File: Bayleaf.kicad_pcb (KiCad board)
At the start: 2 copper layers, 297 x 94.2 mm, 142 parts

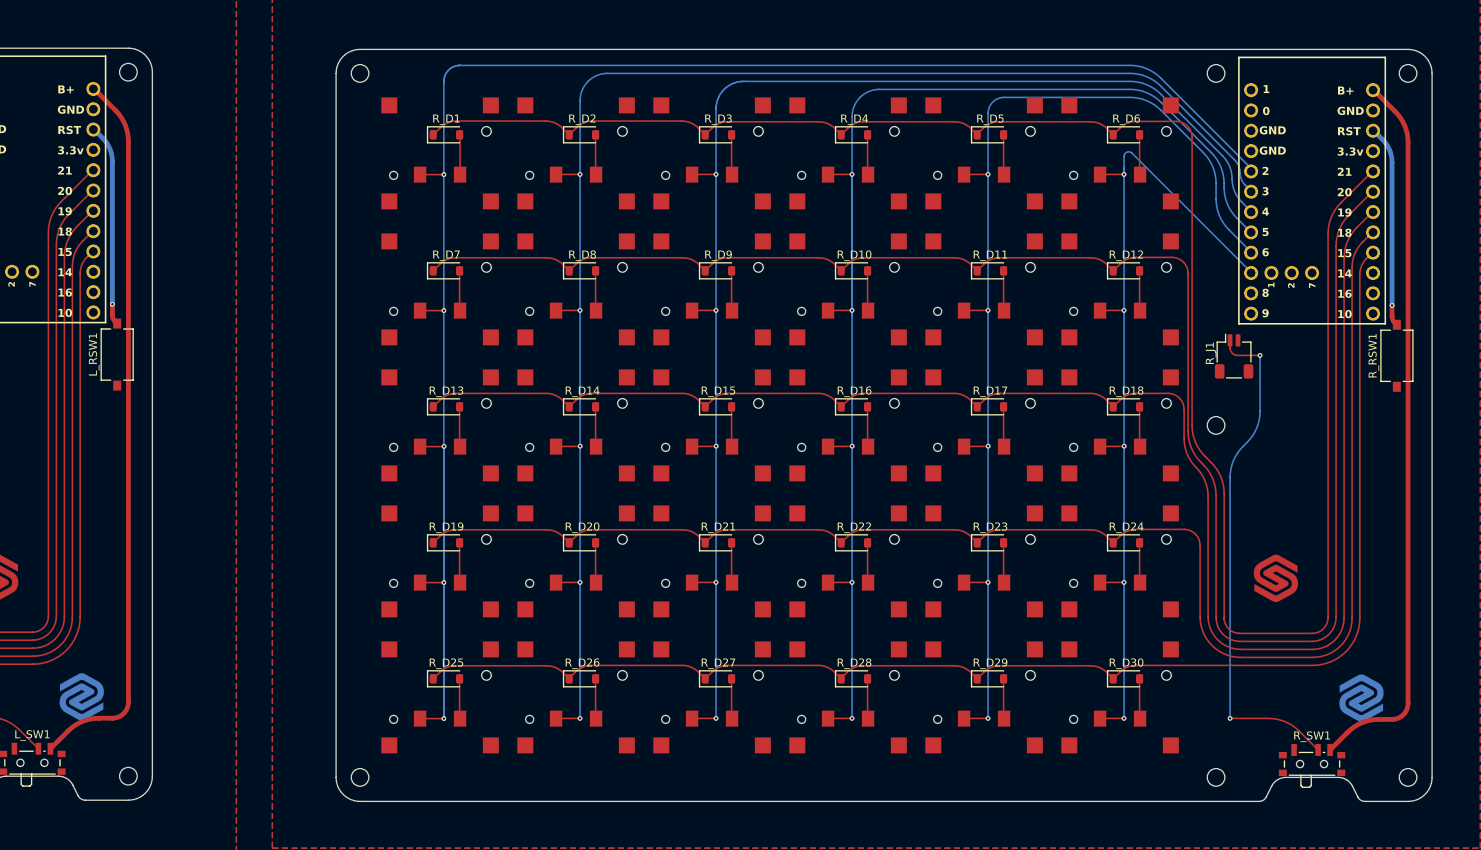
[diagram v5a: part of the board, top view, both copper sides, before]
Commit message: Connect traces on right
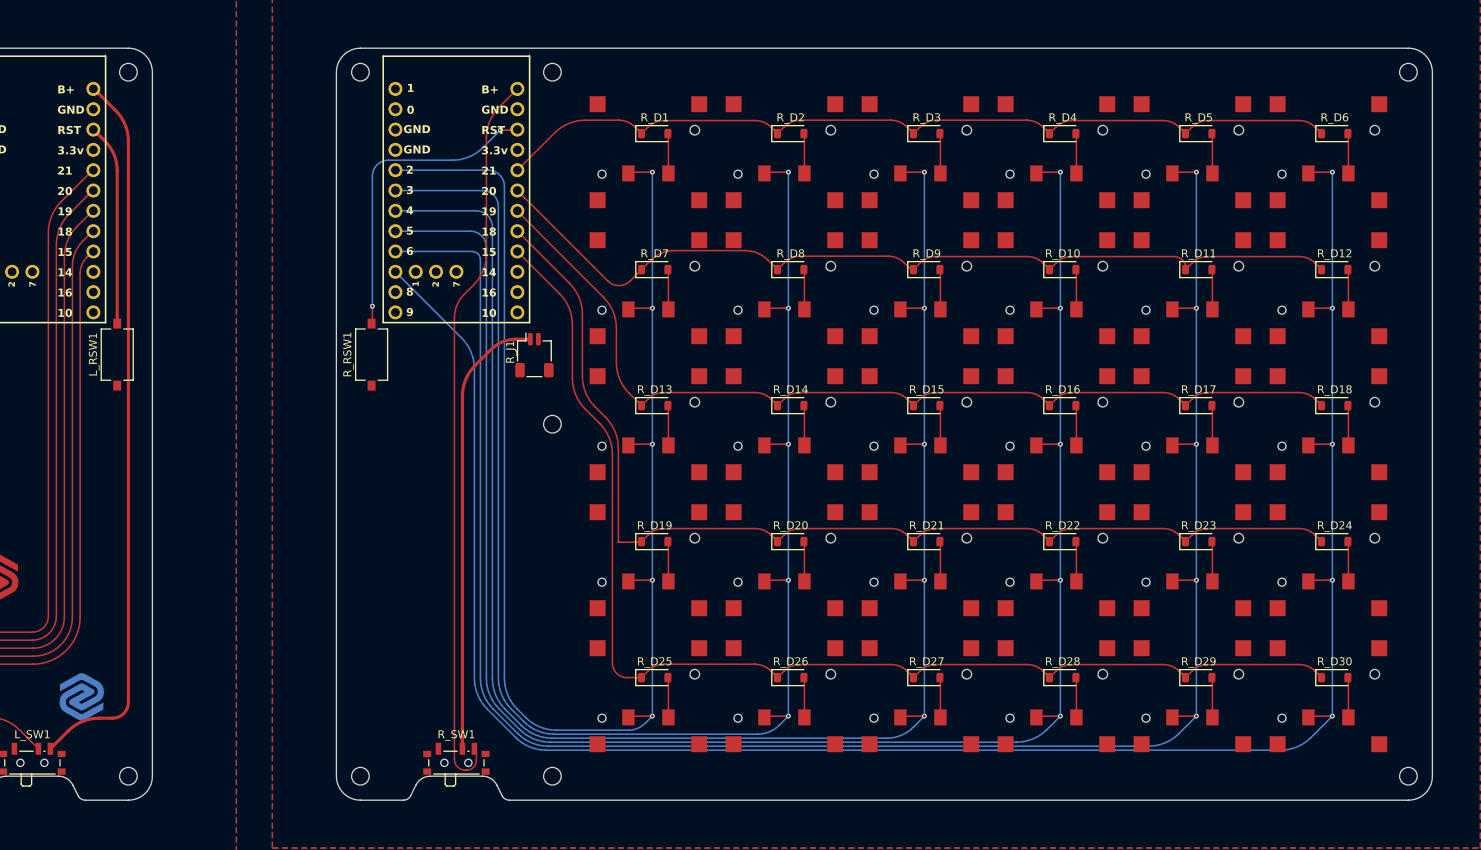
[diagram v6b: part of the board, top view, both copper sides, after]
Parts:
- moved R_RSW1 128.2 mm to (164.4, 38.3)
- moved R_H7 115.7 mm to (187.0, 47.0)
- moved R_H4 115.6 mm to (163.0, 91.0)
- moved R_SW1 107.0 mm to (175.0, 89.0)
- moved R_U1 107.0 mm to (175.0, 18.8)
- moved R_J1 87.5 mm to (184.8, 38.4)
- moved R_H2 83.0 mm to (187.0, 3.00)
- moved R_D12 26.0 mm to (284.8, 27.7)
- moved R_D18 26.0 mm to (284.8, 44.7)
- moved R_D24 26.0 mm to (284.8, 61.7)
- moved R_D30 26.0 mm to (284.8, 78.7)
- moved R_D6 26.0 mm to (284.8, 10.7)
- moved R_S12 26.0 mm to (284.0, 30.0)
- moved R_S18 26.0 mm to (284.0, 47.0)
- moved R_S24 26.0 mm to (284.0, 64.0)
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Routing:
- net col-5R: track 108.3 -> 251.5 mm
- net row-0R: track 236.4 -> 109.1 mm
- net row-1R: track 218.5 -> 112.2 mm
- net col-4R: track 135.4 -> 241.6 mm
- net row-2R: track 201.0 -> 120.7 mm
- net col-3R: track 170.1 -> 226.3 mm
- net col-0R: track 236.1 -> 181.8 mm
- net row-3R: track 185.3 -> 136.9 mm
- net col-2R: track 168.0 -> 211.4 mm
- net row-4R: track 171.3 -> 150.6 mm
- net RESET_R: track 25.3 -> 39.0 mm, vias 1 -> 2
- net col-1R: track 184.6 -> 196.6 mm
- net +BATT: track 64.0 -> 56.4 mm, vias 2 -> 0
- net RAW_R: track 90.4 -> 92.0 mm
- net RESET_L: track 25.3 -> 25.2 mm, vias 1 -> 0
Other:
- board size 297 x 94.2 mm -> 297 x 94 mm

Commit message: Merge boards
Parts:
- added ?: , , F.Cu at (138.0, 10.5)
- added ?: , , F.Cu at (138.0, 80.5)
- added ?: , , F.Cu at (138.0, 83.5)
- added ?: , , F.Cu at (138.0, 13.5)
- added ?: , , F.Cu at (138.0, 12.0)
- added ?: , , F.Cu at (138.0, 82.0)
- moved R_D1 21.0 mm to (178.8, 10.7)
- moved R_D10 21.0 mm to (229.8, 27.7)
- moved R_D11 21.0 mm to (246.8, 27.7)
- moved R_D12 21.0 mm to (263.8, 27.7)
- moved R_D13 21.0 mm to (178.8, 44.7)
- moved R_D14 21.0 mm to (195.8, 44.7)
- moved R_D15 21.0 mm to (212.8, 44.7)
- moved R_D16 21.0 mm to (229.8, 44.7)
- moved R_D17 21.0 mm to (246.8, 44.7)
- moved R_D18 21.0 mm to (263.8, 44.7)
- moved R_D19 21.0 mm to (178.8, 61.7)
- moved R_D2 21.0 mm to (195.8, 10.7)
- moved R_D20 21.0 mm to (195.8, 61.7)
- moved R_D21 21.0 mm to (212.8, 61.7)
- moved R_D22 21.0 mm to (229.8, 61.7)
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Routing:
- net RAW_R: track 92.0 -> 102.1 mm, vias 0 -> 1
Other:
- board size 297 x 94 mm -> 276 x 94 mm
